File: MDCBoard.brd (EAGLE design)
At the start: 43.9 x 32.6 mm, 199 parts, among them J1 JUMPER-SOLDER, J10 MICROSD-SOCKET, J11 USB-C-RECEPTACLE-KOREANHRO, J2 JUMPER-SOLDER, J3 JUMPER-SOLDER, J4 JUMPER-SOLDER, J5 JST-SM02B-SRSS-TB, J6 JUMPER-SOLDER, J7 JUMPER-SOLDER, J8 JUMPER-SOLDER, Q1 PMOS-NEXPERIA-SOT1220, Q2 PMOS-NEXPERIA-SOT1220, Q3 PMOS-NEXPERIA-SOT1220, Q4 DIODESINC-DMG2305UX, Q5 DIODESINC-DMG2305UX, Q6 DIODESINC-DMG2305UX, Q7 DIODESINC-DMG2305UX, Q8 DIODESINC-DMG2305UX, U1 TI-TPS2116, U10 TI-TPS22919DCK, U11 TI-TPS22919DCK, U12 TI-TPS22919DCK, U13 TI-TPS22919DCK, U15 TI-MSP430FR2433IRGE, U16 TI-TXB0102, U17 PANASONIC-EKMB110711X, U18 LATTICE-ICE40HX4K-BG121, U19 WINBOND-W25Q40EW, U2 DIODESINC-AP7350, U20 NEXPERIA-74LVC1G98-OR-INV-INP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, U21 NEXPERIA-74LVC1G98-BUFFER, U22 ON-AR0330CS1C12SPKA0, U23 ALLIANCE-AS4C8M16MSA-6BIN, U24 STM-STM32F730, U25 DIODESINC-DT1446-04V-7, U26 NEXPERIA-74LVC1G98-INVERTER, U3 NEXPERIA-74LVC1G98-NOR, U4 MICROCHIP-MCP7383X, U5 NEXPERIA-74LVC1G98-INVERTER, U6 EATON-STN101, U7 TI-TPS62A01, U8 TI-TPS62A01, U9 TI-TPS62A01, X1 EPSON-FC-135, X2 SITIME-SIT8021, X3 SITIME-SIT8021

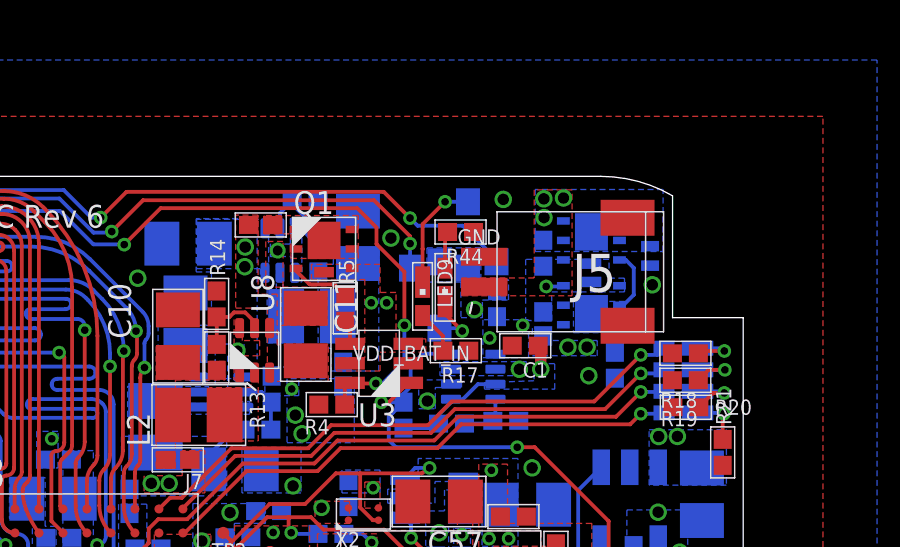
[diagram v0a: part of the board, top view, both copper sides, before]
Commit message: Replace 50Ω resistor with 2x 100Ω resistors
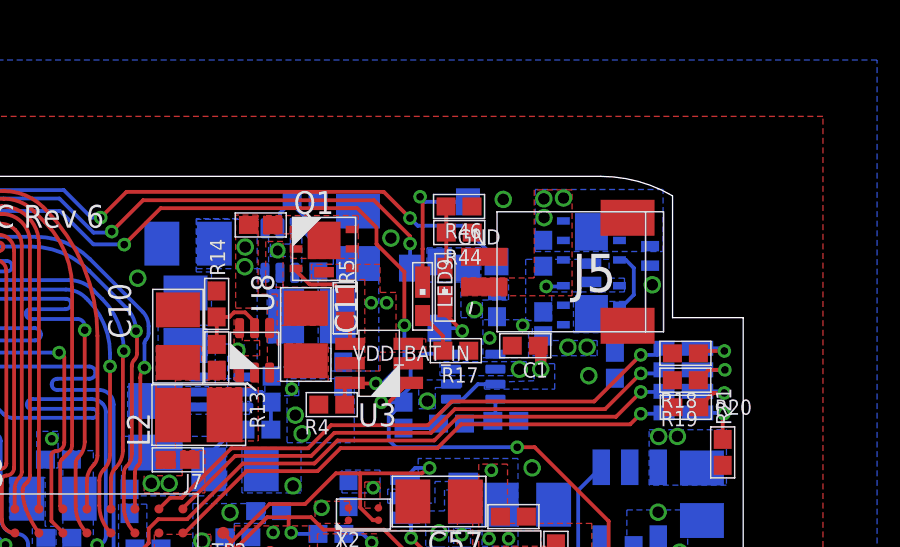
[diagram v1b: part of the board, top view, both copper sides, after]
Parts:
- added R46: 100, EagleLibrary:0402
- R44: value 50 -> 100
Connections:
- net GND: now also R46.1
- net N$45: now also R46.2
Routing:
- net VDD_A: track 45.0 -> 40.8 mm
- net N$45: track 1.24 -> 2.08 mm
- net N$6: track 3.75 -> 4.55 mm
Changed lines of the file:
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@@
 <layer number="13" name="Route13" color="21" fill="1" visible="no" active="no"/>
 <layer number="14" name="Route14" color="22" fill="1" visible="no" active="no"/>
-<layer number="15" name="Power" color="42" fill="1" visible="no" active="yes"/>
-<layer number="16" name="Bottom" color="1" fill="1" visible="yes" active="yes"/>
-<layer number="17" name="Pads" color="2" fill="1" visible="yes" active="yes"/>
+<layer number="15" name="Power" color="42" fill="1" visible="yes" active="yes"/>
+<layer number="16" name="Bottom" color="1" fill="1" visible="no" active="yes"/>
+<layer number="17" name="Pads" color="2" fill="1" visible="no" active="yes"/>
 <layer number="18" name="Vias" color="2" fill="1" visible="yes" active="yes"/>
 <layer number="19" name="Unrouted" color="6" fill="1" visible="no" active="yes"/>
-<layer number="20" name="Dimension" color="24" fill="1" visible="yes" active="yes"/>
+<layer number="20" name="Dimension" color="24" fill="1" visible="no" active="yes"/>
 <layer number="21" name="tPlace" color="7" fill="1" visible="no" active="yes"/>
-<layer number="22" name="bPlace" color="7" fill="1" visible="yes" active="yes"/>
+<layer number="22" name="bPlace" color="7" fill="1" visible="no" active="yes"/>
 <layer number="23" name="tOrigins" color="15" fill="1" visible="no" active="yes"/>
-<layer number="24" name="bOrigins" color="15" fill="1" visible="yes" active="yes"/>
+<layer number="24" name="bOrigins" color="15" fill="1" visible="no" active="yes"/>
 <layer number="25" name="tNames" color="7" fill="1" visible="no" active="yes"/>
-<layer number="26" name="bNames" color="7" fill="1" visible="yes" active="yes"/>
+<layer number="26" name="bNames" color="7" fill="1" visible="no" active="yes"/>
 <layer number="27" name="tValues" color="7" fill="1" visible="no" active="yes"/>
-<layer number="28" name="bValues" color="7" fill="1" visible="yes" active="yes"/>
+<layer number="28" name="bValues" color="7" fill="1" visible="no" active="yes"/>
 <layer number="29" name="tStop" color="7" fill="3" visible="no" active="yes"/>
-<layer number="30" name="bStop" color="7" fill="6" visible="yes" active="yes"/>
+<layer number="30" name="bStop" color="7" fill="6" visible="no" active="yes"/>
 <layer number="31" name="tCream" color="7" fill="4" visible="no" active="yes"/>
-<layer number="32" name="bCream" color="7" fill="5" visible="yes" active="yes"/>
+<layer number="32" name="bCream" color="7" fill="5" visible="no" active="yes"/>
 <layer number="33" name="tFinish" color="6" fill="3" visible="no" active="yes"/>
-<layer number="34" name="bFinish" color="6" fill="6" visible="yes" active="yes"/>
+<layer number="34" name="bFinish" color="6" fill="6" visible="no" active="yes"/>
 <layer number="35" name="tGlue" color="7" fill="4" visible="no" active="yes"/>
-<layer number="36" name="bGlue" color="7" fill="5" visible="yes" active="yes"/>
+<layer number="36" name="bGlue" color="7" fill="5" visible="no" active="yes"/>
 <layer number="37" name="tTest" color="7" fill="1" visible="no" active="yes"/>
-<layer number="38" name="bTest" color="7" fill="1" visible="yes" active="yes"/>
+<layer number="38" name="bTest" color="7" fill="1" visible="no" active="yes"/>
 <layer number="39" name="tKeepout" color="4" fill="11" visible="no" active="yes"/>
-<layer number="40" name="bKeepout" color="1" fill="11" visible="yes" active="yes"/>
+<layer number="40" name="bKeepout" color="1" fill="11" visible="no" active="yes"/>
 <layer number="41" name="tRestrict" color="4" fill="10" visible="no" active="yes"/>
-<layer number="42" name="bRestrict" color="1" fill="10" visible="yes" active="yes"/>
+<layer number="42" name="bRestrict" color="1" fill="10" visible="no" active="yes"/>
 <layer number="43" name="vRestrict" color="2" fill="10" visible="no" active="yes"/>
 <layer number="44" name="Drills" color="7" fill="1" visible="no" active="yes"/>
@@
 <attribute name="PN" value="DMG2305UX" x="4.046221875" y="20.43938125" size="1.778" layer="28" rot="MR180" display="off"/>
 </element>
-<element name="R44" library="EagleLibrary" package="0402" value="50" x="34.433340625" y="30.795359375" smashed="yes" rot="R180">
-<attribute name="MFG" value="" x="34.433340625" y="30.795359375" size="1.778" layer="27" rot="R180" display="off"/>
-<attribute name="NAME" x="35.187340625" y="30.239359375" size="0.508" layer="25" font="vector" rot="R180"/>
-<attribute name="PN" value="" x="34.433340625" y="30.795359375" size="1.778" layer="27" rot="R180" display="off"/>
-</element>
 <element name="U15" library="EagleLibrary" package="TI-MSP430FR2433IRGE" value="TI-MSP430FR2433IRGE" x="11.654" y="3.792" smashed="yes" rot="R270">
 <attribute name="MFG" value="Texas Instruments" x="11.654" y="3.792" size="1.778" layer="27" rot="R270" display="off"/>
@@
 <attribute name="PN" value="MSP430FR2433IRGE" x="11.654" y="3.792" size="1.778" layer="27" rot="R270" display="off"/>
 </element>
+<element name="R44" library="EagleLibrary" package="0402" value="100" x="34.39" y="30.775" smashed="yes" rot="R180">
+<attribute name="MFG" value="" x="34.39" y="30.775" size="1.778" layer="27" rot="R180" display="off"/>
+<attribute name="NAME" x="35.144" y="30.219" size="0.508" layer="25" font="vector" rot="R180"/>
+<attribute name="PN" value="" x="34.39" y="30.775" size="1.778" layer="27" rot="R180" display="off"/>
+</element>
+<element name="R46" library="EagleLibrary" package="0402" value="100" x="34.384" y="31.646" smashed="yes" rot="R180">
+<attribute name="MFG" value="" x="34.384" y="31.646" size="1.778" layer="27" rot="R180" display="off"/>
+<attribute name="NAME" x="35.138" y="31.09" size="0.508" layer="25" font="vector" rot="R180"/>
+<attribute name="PN" value="" x="34.384" y="31.646" size="1.778" layer="27" rot="R180" display="off"/>
+</element>
 </elements>
 <signals>
@@
 <contactref element="R17" pad="1"/>
 <contactref element="U5" pad="6"/>
-<contactref element="R44" pad="1"/>
 <via x="29.8" y="21.6" extent="1-16" drill="0.35"/>
 <polygon width="0.127" layer="1">
@@
 <via x="35.85718125" y="31.88208125" extent="1-16" drill="0.381"/>
 <via x="36.50488125" y="27.686" extent="1-16" drill="0.254"/>
+<contactref element="R44" pad="1"/>
+<contactref element="R46" pad="1"/>
 </signal>
 <signal name="ICE_IMG_CLK16MHZ">
@@
 <wire x1="5.9582625" y1="31.161578125" x2="5.9582625" y2="29.164703125" width="0.381" layer="15"/>
 <wire x1="5.4006" y1="28.607040625" x2="5.9582625" y2="29.164703125" width="0.381" layer="15"/>
-<wire x1="6.696459375" y1="31.950659375" x2="33.3709" y2="31.950659375" width="0.381" layer="15"/>
+<wire x1="30.8309" y1="31.950659375" x2="6.696459375" y2="31.950659375" width="0.381" layer="15"/>
 <wire x1="6.696459375" y1="31.950659375" x2="5.9582625" y2="31.2124625" width="0.381" layer="15"/>
 <wire x1="5.9582625" y1="31.161578125" x2="5.9582625" y2="31.2124625" width="0.381" layer="15"/>
@@
 <via x="31.457896875" y="28.4353" extent="1-16" drill="0.254"/>
 <wire x1="31.457896875" y1="28.4353" x2="31.968440625" y2="28.4353" width="0.381" layer="15"/>
-<wire x1="33.3709" y1="31.950659375" x2="33.3709" y2="31.2569" width="0.381" layer="15"/>
-<wire x1="33.3709" y1="31.2569" x2="36.3954" y2="31.2569" width="0.381" layer="15"/>
-<wire x1="36.3954" y1="31.2569" x2="36.3954" y2="29.464" width="0.381" layer="15"/>
 <wire x1="31.968440625" y1="28.4353" x2="32.997140625" y2="29.464" width="0.381" layer="15"/>
 <wire x1="32.997140625" y1="29.464" x2="36.3954" y2="29.464" width="0.381" layer="15"/>
@@
 <wire x1="35.9537" y1="29.0223" x2="36.3954" y2="29.464" width="0.381" layer="15"/>
 <wire x1="35.9537" y1="26.6623" x2="35.9537" y2="29.0223" width="0.381" layer="15"/>
+<wire x1="31.457896875" y1="28.4353" x2="30.8309" y2="29.062296875" width="0.381" layer="15"/>
+<wire x1="30.8309" y1="29.062296875" x2="30.8309" y2="31.950659375" width="0.381" layer="15"/>
 </signal>
 <signal name="N$42">
@@
 <contactref element="Q6" pad="D"/>
 <contactref element="LED9" pad="A"/>
-<wire x1="34.681159375" y1="31.802578125" x2="33.917421875" y2="31.802578125" width="0.127" layer="16"/>
-<wire x1="33.917421875" y1="31.802578125" x2="33.917" y2="31.803" width="0.127" layer="16"/>
-<via x="33.917" y="31.803" extent="1-16" drill="0.254"/>
+<wire x1="34.681159375" y1="31.802578125" x2="33.250421875" y2="31.802578125" width="0.127" layer="16"/>
+<wire x1="33.250421875" y1="31.802578125" x2="33.084" y2="31.969" width="0.127" layer="16"/>
+<via x="33.084" y="31.969" extent="1-16" drill="0.254"/>
 <wire x1="33.1698625" y1="30.23528125" x2="33.1674" y2="30.23281875" width="0.127" layer="1"/>
 <wire x1="33.1674" y1="30.23281875" x2="33.1674" y2="29.125" width="0.127" layer="1"/>
-<wire x1="33.917" y1="31.803" x2="33.1698625" y2="31.0558625" width="0.127" layer="1"/>
-<wire x1="33.1698625" y1="31.0558625" x2="33.1698625" y2="30.23528125" width="0.127" layer="1"/>
+<wire x1="33.084" y1="31.969" x2="33.1698625" y2="31.8831375" width="0.127" layer="1"/>
+<wire x1="33.1698625" y1="31.8831375" x2="33.1698625" y2="30.23528125" width="0.127" layer="1"/>
 </signal>
 <signal name="LED_FLASH_RED_">
@@
 <contactref element="LED11" pad="C"/>
 <contactref element="R44" pad="2"/>
-<wire x1="33.9174" y1="29.59" x2="33.9174" y2="30.71191875" width="0.127" layer="1"/>
-<wire x1="33.9174" y1="30.71191875" x2="34.000840625" y2="30.795359375" width="0.127" layer="1"/>
+<contactref element="R46" pad="2"/>
+<wire x1="33.9515" y1="31.646" x2="33.9575" y2="31.64" width="0.127" layer="1"/>
+<wire x1="33.9575" y1="31.64" x2="33.9575" y2="30.775" width="0.127" layer="1"/>
+<wire x1="33.9575" y1="30.775" x2="33.9575" y2="29.6301" width="0.127" layer="1"/>
+<wire x1="33.9575" y1="29.6301" x2="33.9174" y2="29.59" width="0.127" layer="1"/>
 </signal>
 <signal name="LED_FLASH_GREEN_">

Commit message: Preparing to add button
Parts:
- moved R39 0.57 mm to (36.8, 3.92), turned to 180 degrees
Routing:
- net N$54: track 14.1 -> 13.1 mm, vias 1 -> 2

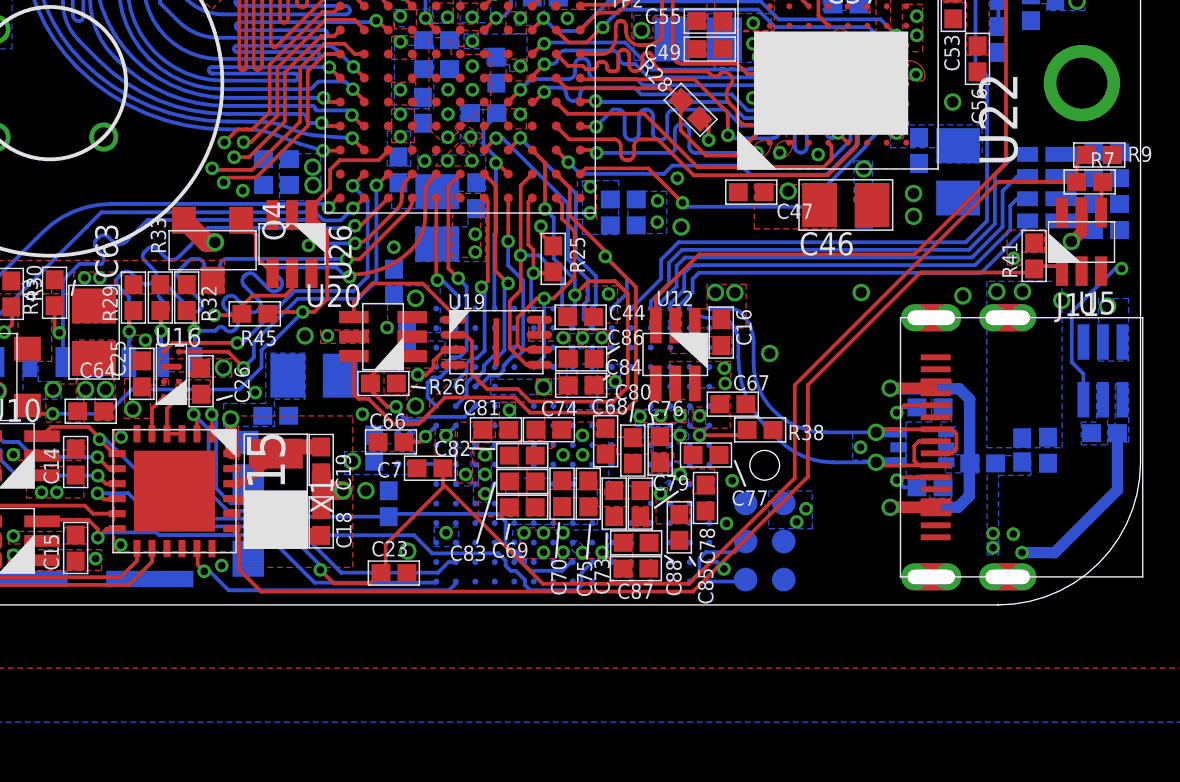
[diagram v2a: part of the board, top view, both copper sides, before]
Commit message: - Added button - Routed BUTTON_SIGNAL_ to MSP - Updated bypass caps for STM's 3V3 signals
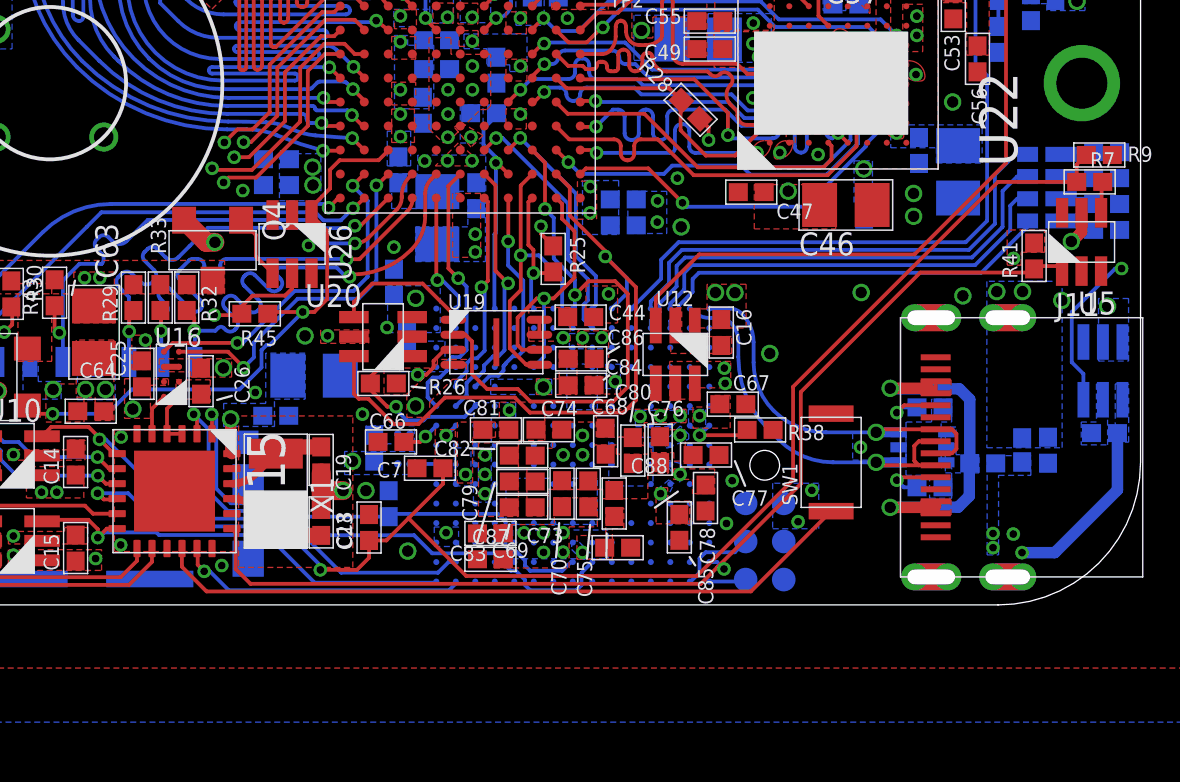
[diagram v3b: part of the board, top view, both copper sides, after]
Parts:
- added SW1: TACTILE-SWITCH, EagleLibrary:DEALON-TD-1624UR-180
- moved C79 5.10 mm to (22.2, 2.38), turned to 180 degrees
- moved C87 4.86 mm to (22.2, 1.52), turned to 180 degrees
- moved C23 1.73 mm to (18.1, 2.58), turned to 90 degrees
- moved C88 1.50 mm to (26.3, 3.38), turned to 90 degrees
- moved C73 1.48 mm to (26.4, 1.91), turned to 0 degrees
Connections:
- new net BUTTON_SIGNAL_: SW1.1, U15.16
- net GND: now also SW1.2
- net VDD_B_1V8_STM: no longer C73.1, C88.1
- net VDD_B_3V3_STM: now also C73.1, C88.1
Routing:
- net BUTTON_SIGNAL_: track 0.00 -> 23.7 mm
- net VDD_USB_IN: track 8.13 -> 8.75 mm
- net VDD_A_3V3: track 132.1 -> 132.6 mm
- net VDD_B_1V8_STM: vias 21 -> 20

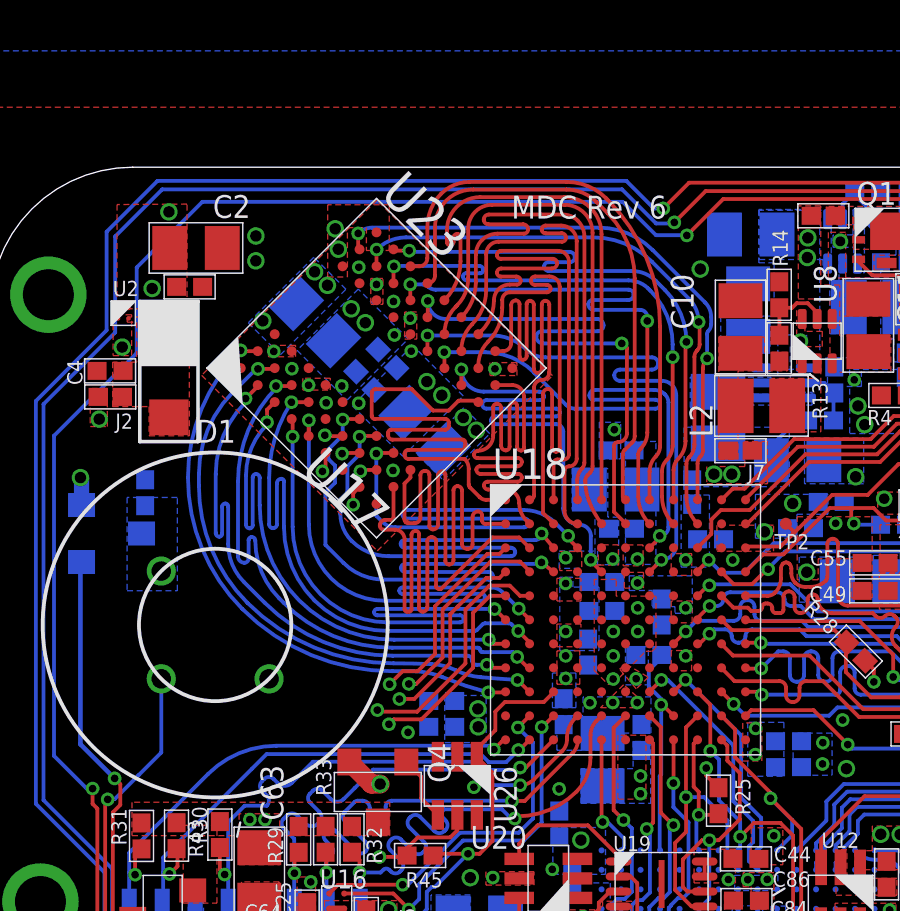
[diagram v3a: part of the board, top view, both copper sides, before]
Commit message: Reimplemented RAM routing
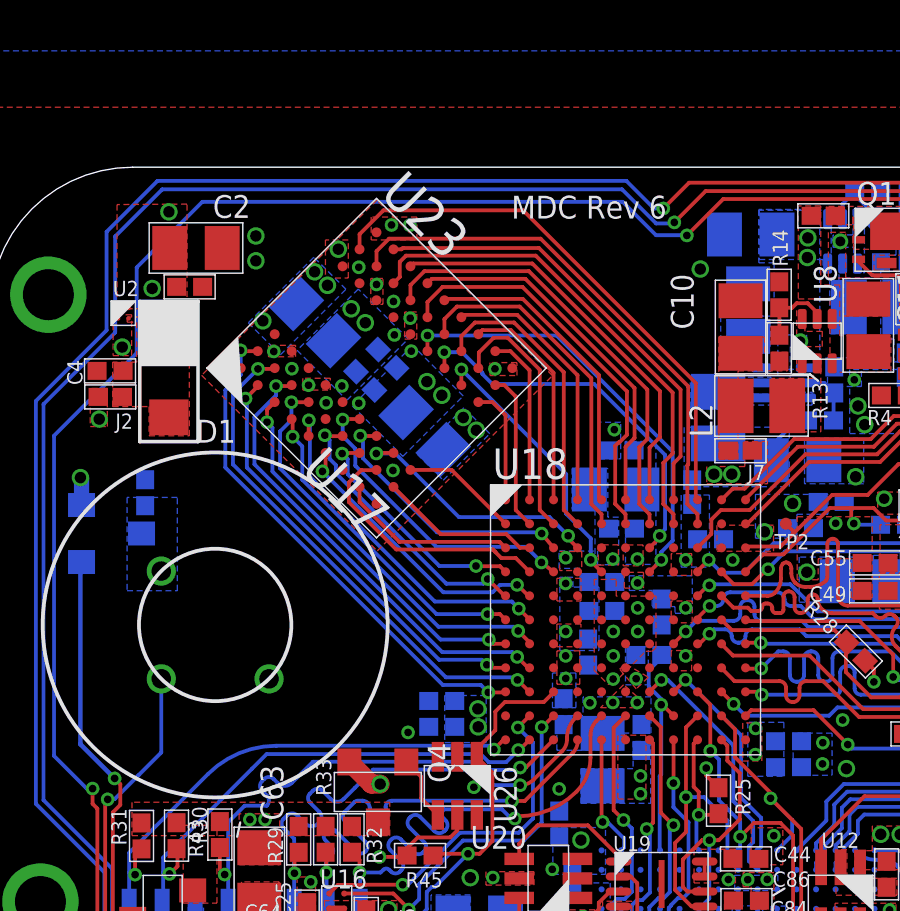
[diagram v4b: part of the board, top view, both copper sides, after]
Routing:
- net RAM_A3: track 19.1 -> 3.95 mm
- net RAM_A4: track 18.9 -> 3.91 mm
- net RAM_A5: track 19.0 -> 5.38 mm
- net RAM_A2: track 18.6 -> 5.27 mm
- net RAM_A10: track 18.2 -> 5.72 mm
- net RAM_CS_: track 18.5 -> 7.39 mm
- net RAM_A9: track 19.4 -> 8.95 mm
- net RAM_A1: track 18.6 -> 8.53 mm
- net RAM_A6: track 18.6 -> 8.64 mm
- net RAM_WE_: track 18.6 -> 8.89 mm
- net RAM_A0: track 18.7 -> 9.20 mm
- net RAM_CLK: track 18.8 -> 9.51 mm
- net RAM_CKE: track 19.6 -> 10.3 mm
- net RAM_BA1: track 18.4 -> 10.0 mm
- net RAM_A11: track 16.1 -> 7.96 mm
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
